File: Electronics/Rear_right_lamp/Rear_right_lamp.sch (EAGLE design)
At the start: 10 parts, among them X2 JST-XH-05-PIN-LONG-PAD

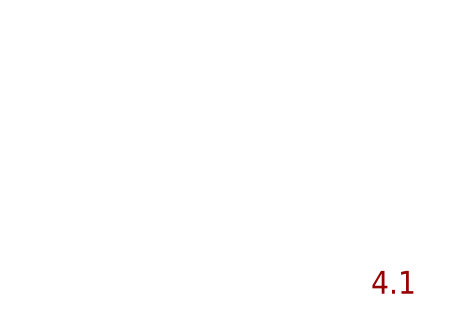
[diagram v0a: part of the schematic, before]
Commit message: Rear lamps improved
What has been improved:
- changed API_START_ENGINE red LEDs' CURRENT_EMPIRICAL value one decimal point smaller
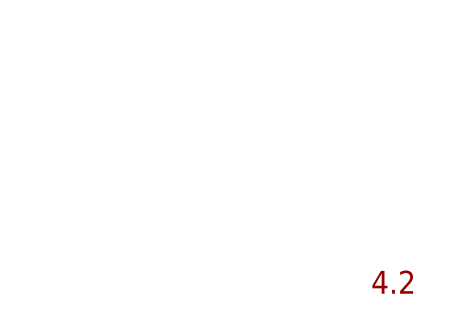
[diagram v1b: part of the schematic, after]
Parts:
- LED1, LED2: CURRENT_EMPIRICAL 1.48 mA -> 0.15 mA
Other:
- note added: "4.2"
- note removed: "4.1"
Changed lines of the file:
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@@
 <part name="LED1" library="led" deviceset="LED" device="5MM" value="Red">
 <attribute name="COLOR" value="Red"/>
-<attribute name="CURRENT_EMPIRICAL" value="1.48 mA"/>
+<attribute name="CURRENT_EMPIRICAL" value="0.15 mA"/>
 <attribute name="MANUFACTURER" value="LUCKYLIGHT"/>
 <attribute name="MANUFACTURER_PART_NUMBER" value="LL-503VD2E-1B"/>
@@
 <part name="LED2" library="led" deviceset="LED" device="5MM" value="Red">
 <attribute name="COLOR" value="Red"/>
-<attribute name="CURRENT_EMPIRICAL" value="1.48 mA"/>
+<attribute name="CURRENT_EMPIRICAL" value="0.15 mA"/>
 <attribute name="MANUFACTURER" value="LUCKYLIGHT"/>
 <attribute name="MANUFACTURER_PART_NUMBER" value="LL-503VD2E-1B"/>
@@
 <text x="175.26" y="27.94" size="2.54" layer="94">Author: sesame0707</text>
 <text x="205.994" y="11.43" size="2.54" layer="94">4</text>
-<text x="261.62" y="7.112" size="2.54" layer="94">4.1</text>
+<text x="261.62" y="7.112" size="2.54" layer="94">4.2</text>
 </plain>
 <instances>
